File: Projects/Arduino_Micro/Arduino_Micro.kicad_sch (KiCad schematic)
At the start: 2 parts, among them J1 Analog, J2 Digital

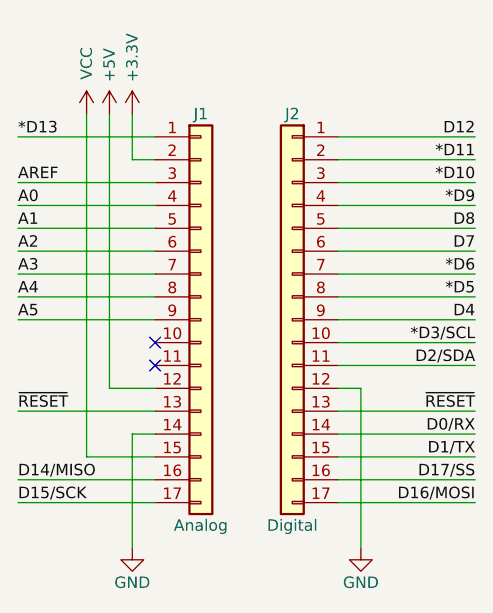
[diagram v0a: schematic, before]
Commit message: Update templates to V8 format
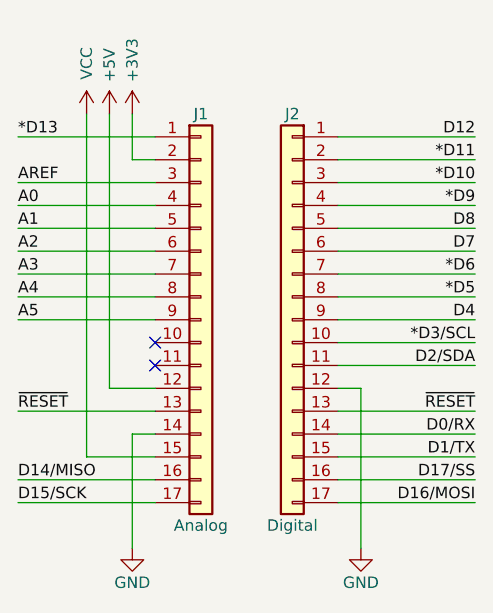
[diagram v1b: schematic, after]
